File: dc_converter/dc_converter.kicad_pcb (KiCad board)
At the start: 2 copper layers, 58 x 42.5 mm, 39 parts, among them IC1 A3946KLPTR-T, IC2 NCV20072DMR2G, J1 xt30Con, J2 xt30Con, J3 Conn_01x09_Pin, Q1 CSD18531Q5A, Q2 CSD18531Q5A, Q3 CSD18531Q5A, U1 LM74700, U3 INA280A2xDCK, U4 INA280A2xDCK

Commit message: Added 2 simulink concepts, with high and low sides mosfets
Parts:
- R1, R2: footprint Resistor_SMD:R_0402_1005Metric -> Resistor_SMD:R_1206_3216Metric_Pad1.30x1.75mm_HandSolder
- moved R2 15.3 mm to (118.5, 86.5), turned to -90 degrees
- moved R1 10.6 mm to (122.5, 86.5), turned to -90 degrees
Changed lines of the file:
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@@
 		)
 	)
-	(footprint "Resistor_SMD:R_0402_1005Metric"
+	(footprint "Resistor_SMD:R_1206_3216Metric_Pad1.30x1.75mm_HandSolder"
 		(layer "F.Cu")
-		(at 127.5 77.15)
-		(descr "Resistor SMD 0402 (1005 Metric), square (rectangular) end terminal, IPC-7351 nominal, (Body size source: IPC-SM-782 page 72, https://www.pcb-3d.com/wordpress/wp-content/uploads/ipc-sm-782a_amendment_1_and_2.pdf)")
-		(tags "resistor")
+		(at 122.5 86.45 -90)
+		(descr "Resistor SMD 1206 (3216 Metric), square (rectangular) end terminal, IPC-7351 nominal with elongated pad for handsoldering. (Body size source: IPC-SM-782 page 72, https://www.pcb-3d.com/wordpress/wp-content/uploads/ipc-sm-782a_amendment_1_and_2.pdf)")
+		(tags "resistor handsolder")
 		(property "Reference" "R1"
-			(at 2 0 0)
+			(at 0 -1.83 90)
 			(layer "F.SilkS")
 			(effects
@@
 		)
 		(property "Value" "33Ω"
-			(at 0 1.17 0)
+			(at 0 1.83 90)
 			(layer "F.Fab")
 			(effects
@@
 		)
 		(property "Datasheet" ""
-			(at 0 0 0)
+			(at 0 0 90)
 			(layer "F.Fab")
 			(hide yes)
@@
 		)
 		(property "Description" "Resistor"
-			(at 0 0 0)
+			(at 0 0 90)
 			(layer "F.Fab")
 			(hide yes)
@@
 		)
 		(property "KiLib_Generator" "SMD_2terminal_chip_molded"
-			(at 0 0 0)
+			(at 0 0 90)
 			(layer "F.SilkS")
 			(hide yes)
@@
 		(duplicate_pad_numbers_are_jumpers no)
 		(fp_line
-			(start -0.153641 -0.38)
-			(end 0.153641 -0.38)
-			(stroke
-				(width 0.12)
-				(type solid)
-			)
-			(layer "F.SilkS")
-		)
-		(fp_line
-			(start -0.153641 0.38)
-			(end 0.153641 0.38)
+			(start -0.727064 0.91)
+			(end 0.727064 0.91)
+			(stroke
+				(width 0.12)
+				(type solid)
+			)
+			(layer "F.SilkS")
+		)
+		(fp_line
+			(start -0.727064 -0.91)
+			(end 0.727064 -0.91)
 			(stroke
 				(width 0.12)
@@
 		)
 		(fp_rect
-			(start -0.93 -0.47)
-			(end 0.93 0.47)
+			(start -2.45 -1.13)
+			(end 2.45 1.13)
 			(stroke
 				(width 0.05)
@@
 		)
 		(fp_rect
-			(start -0.525 -0.27)
-			(end 0.525 0.27)
+			(start -1.6 -0.8)
+			(end 1.6 0.8)
 			(stroke
 				(width 0.1)
@@
 		)
 		(fp_text user "${REFERENCE}"
-			(at 0 0 0)
-			(layer "F.Fab")
-			(effects
-				(font
-					(size 0.26 0.26)
-					(thickness 0.04)
+			(at 0 0 90)
+			(layer "F.Fab")
+			(effects
+				(font
+					(size 0.8 0.8)
+					(thickness 0.12)
 				)
 			)
 		)
 		(pad "1" smd roundrect
-			(at -0.51 0)
-			(size 0.54 0.64)
-			(layers "F.Cu" "F.Mask" "F.Paste")
-			(roundrect_rratio 0.25)
+			(at -1.55 0 270)
+			(size 1.3 1.75)
+			(layers "F.Cu" "F.Mask" "F.Paste")
+			(roundrect_rratio 0.192308)
 			(net "Net-(IC1-GL)")
 			(pintype "passive")
 		)
 		(pad "2" smd roundrect
-			(at 0.51 0)
-			(size 0.54 0.64)
-			(layers "F.Cu" "F.Mask" "F.Paste")
-			(roundrect_rratio 0.25)
+			(at 1.55 0 270)
+			(size 1.3 1.75)
+			(layers "F.Cu" "F.Mask" "F.Paste")
+			(roundrect_rratio 0.192308)
 			(net "Net-(Q2-G)")
 			(pintype "passive")
 		)
 		(embedded_fonts no)
-		(model "${KICAD10_3DMODEL_DIR}/Resistor_SMD.3dshapes/R_0402_1005Metric.step"
+		(model "${KICAD10_3DMODEL_DIR}/Resistor_SMD.3dshapes/R_1206_3216Metric.step"
 			(offset
 				(xyz 0 0 0)
@@
 		)
 	)
-	(footprint "Resistor_SMD:R_0402_1005Metric"
+	(footprint "Resistor_SMD:R_1206_3216Metric_Pad1.30x1.75mm_HandSolder"
 		(layer "F.Cu")
-		(at 127.5 74.15)
-		(descr "Resistor SMD 0402 (1005 Metric), square (rectangular) end terminal, IPC-7351 nominal, (Body size source: IPC-SM-782 page 72, https://www.pcb-3d.com/wordpress/wp-content/uploads/ipc-sm-782a_amendment_1_and_2.pdf)")
-		(tags "resistor")
+		(at 118.5 86.5 -90)
+		(descr "Resistor SMD 1206 (3216 Metric), square (rectangular) end terminal, IPC-7351 nominal with elongated pad for handsoldering. (Body size source: IPC-SM-782 page 72, https://www.pcb-3d.com/wordpress/wp-content/uploads/ipc-sm-782a_amendment_1_and_2.pdf)")
+		(tags "resistor handsolder")
 		(property "Reference" "R2"
-			(at 2 0 0)
+			(at 0 -1.83 90)
 			(layer "F.SilkS")
 			(effects
@@
 		)
 		(property "Value" "33Ω"
-			(at 0 1.17 0)
+			(at 0 1.83 90)
 			(layer "F.Fab")
 			(effects
@@
 		)
 		(property "Datasheet" ""
-			(at 0 0 0)
+			(at 0 0 90)
 			(layer "F.Fab")
 			(hide yes)
@@
 		)
 		(property "Description" "Resistor"
-			(at 0 0 0)
+			(at 0 0 90)
 			(layer "F.Fab")
 			(hide yes)
@@
 		)
 		(property "KiLib_Generator" "SMD_2terminal_chip_molded"
-			(at 0 0 0)
+			(at 0 0 90)
 			(layer "F.SilkS")
 			(hide yes)
@@
 		(duplicate_pad_numbers_are_jumpers no)
 		(fp_line
-			(start -0.153641 -0.38)
-			(end 0.153641 -0.38)
-			(stroke
-				(width 0.12)
-				(type solid)
-			)
-			(layer "F.SilkS")
-		)
-		(fp_line
-			(start -0.153641 0.38)
-			(end 0.153641 0.38)
+			(start -0.727064 0.91)
+			(end 0.727064 0.91)
+			(stroke
+				(width 0.12)
+				(type solid)
+			)
+			(layer "F.SilkS")
+		)
+		(fp_line
+			(start -0.727064 -0.91)
+			(end 0.727064 -0.91)
 			(stroke
 				(width 0.12)
@@
 		)
 		(fp_rect
-			(start -0.93 -0.47)
-			(end 0.93 0.47)
+			(start -2.45 -1.13)
+			(end 2.45 1.13)
 			(stroke
 				(width 0.05)
@@
 		)
 		(fp_rect
-			(start -0.525 -0.27)
-			(end 0.525 0.27)
+			(start -1.6 -0.8)
+			(end 1.6 0.8)
 			(stroke
 				(width 0.1)
@@
 		)
 		(fp_text user "${REFERENCE}"
-			(at 0 0 0)
-			(layer "F.Fab")
-			(effects
-				(font
-					(size 0.26 0.26)
-					(thickness 0.04)
+			(at 0 0 90)
+			(layer "F.Fab")
+			(effects
+				(font
+					(size 0.8 0.8)
+					(thickness 0.12)
 				)
 			)
 		)
 		(pad "1" smd roundrect
-			(at -0.51 0)
-			(size 0.54 0.64)
-			(layers "F.Cu" "F.Mask" "F.Paste")
-			(roundrect_rratio 0.25)
+			(at -1.55 0 270)
+			(size 1.3 1.75)
+			(layers "F.Cu" "F.Mask" "F.Paste")
+			(roundrect_rratio 0.192308)
 			(net "Net-(IC1-GH)")
 			(pintype "passive")
 		)
 		(pad "2" smd roundrect
-			(at 0.51 0)
-			(size 0.54 0.64)
-			(layers "F.Cu" "F.Mask" "F.Paste")
-			(roundrect_rratio 0.25)
+			(at 1.55 0 270)
+			(size 1.3 1.75)
+			(layers "F.Cu" "F.Mask" "F.Paste")
+			(roundrect_rratio 0.192308)
 			(net "Net-(Q1-G)")
 			(pintype "passive")
 		)
 		(embedded_fonts no)
-		(model "${KICAD10_3DMODEL_DIR}/Resistor_SMD.3dshapes/R_0402_1005Metric.step"
+		(model "${KICAD10_3DMODEL_DIR}/Resistor_SMD.3dshapes/R_1206_3216Metric.step"
 			(offset
 				(xyz 0 0 0)

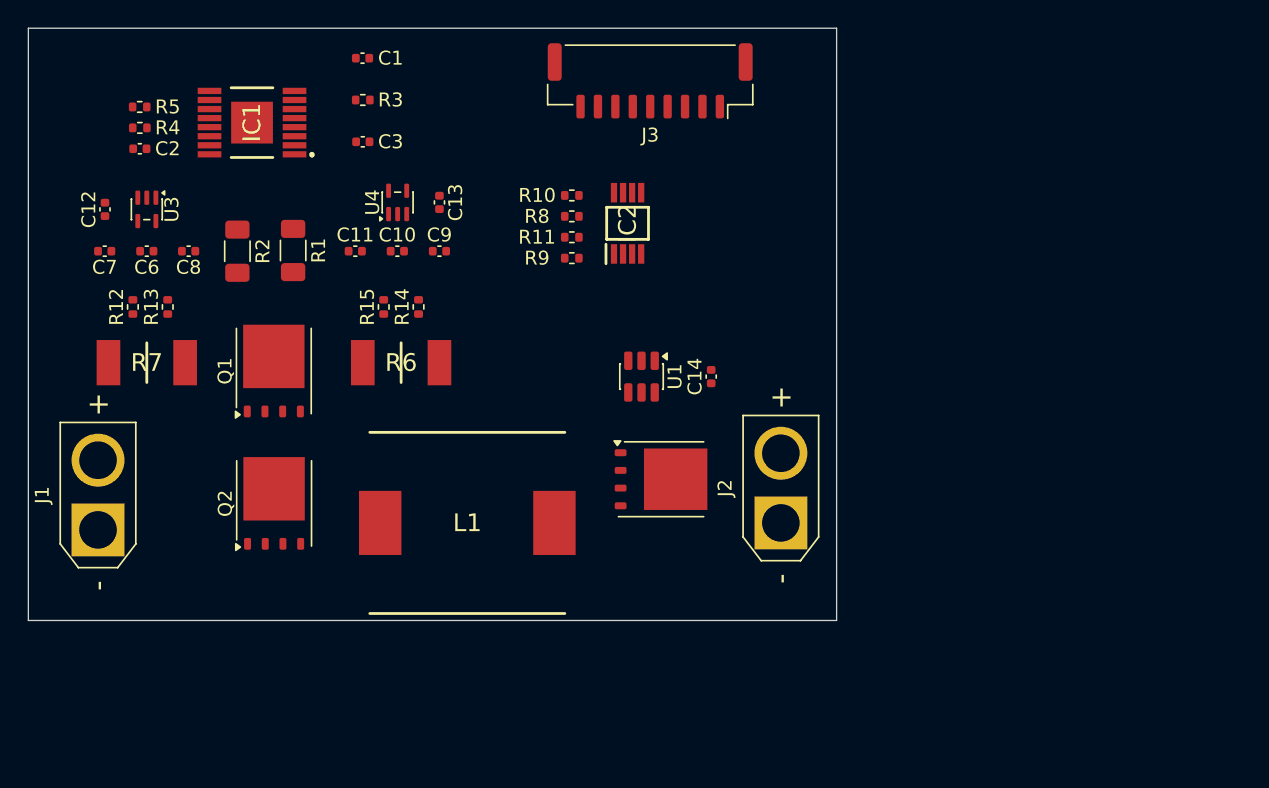
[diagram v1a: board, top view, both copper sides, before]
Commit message: Full topology change to the circuit, diode for Q2, new L, new driver, topology changes in simulink
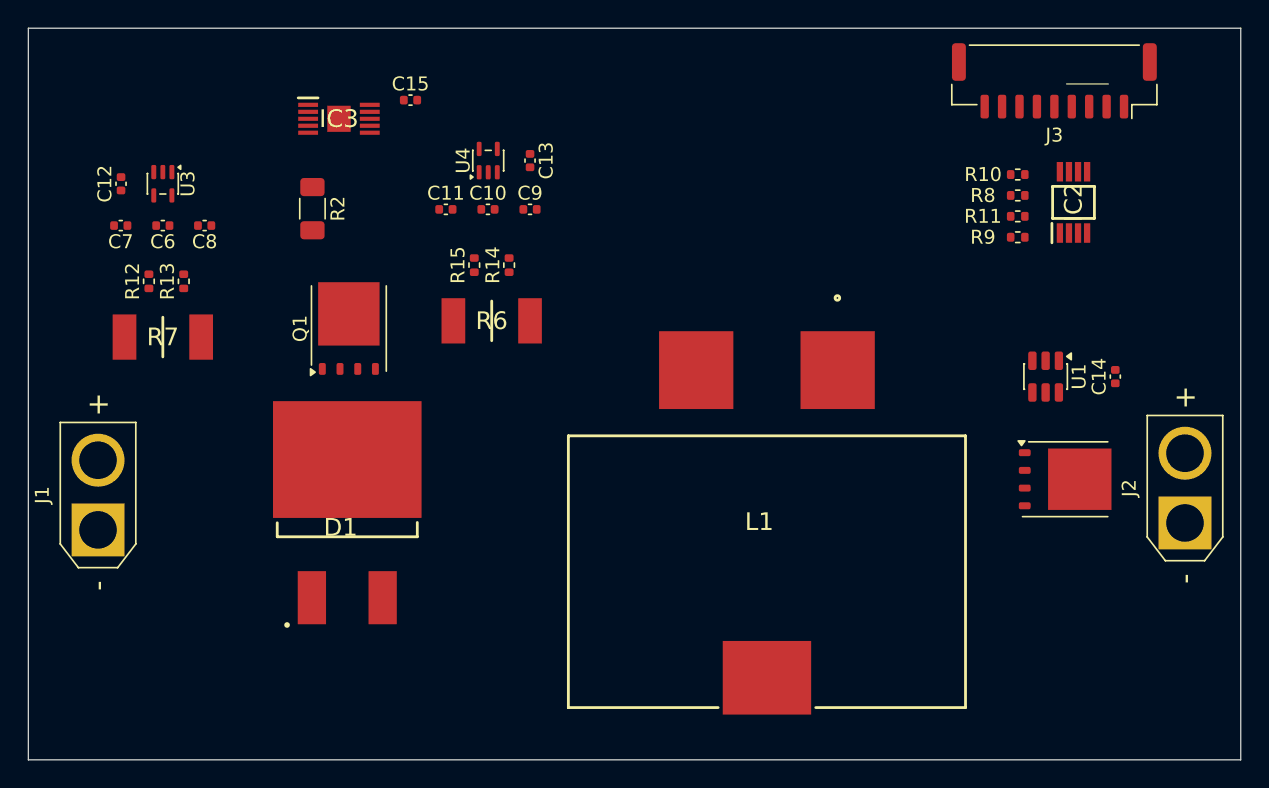
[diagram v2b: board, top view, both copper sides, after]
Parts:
- removed C1, C3: 470nF, Capacitor_SMD:C_0402_1005Metric
- removed C2: 100nF, Capacitor_SMD:C_0402_1005Metric
- removed IC1: A3946KLPTR-T, A3946KLPTR-T:A2550KLPTRT
- removed Q2: CSD18531Q5A, Package_TO_SOT_SMD:TDSON-8-1
- removed R1: 33Ω, Resistor_SMD:R_1206_3216Metric_Pad1.30x1.75mm_HandSolder
- removed R3: 470kΩ, Resistor_SMD:R_0402_1005Metric
- removed R4: 10kΩ, Resistor_SMD:R_0402_1005Metric
- removed R5: 15.8kΩ, Resistor_SMD:R_0402_1005Metric
- added C15: 100nF, Capacitor_SMD:C_0402_1005Metric, F.Cu at (130.9, 75.7)
- added D1: VBT3045C-E3_8W, VBT3045C-E3_8W:TO-263AB_1, F.Cu at (121.4, 98.4)
- added IC3: LTC7004HMSE#TRPBF, LTC7004HMSE:SOP50P490X110-11N, F.Cu at (125.8, 77.0)
- L1: value 744309025 -> 7443641000; footprint 744309025:INDPM140130X900N -> 7443641000:WE-HCF_SMD_HIGH-CURRENT_INDUCTOR
- R2: value 33Ω -> 4.7Ω
- moved IC2 32.0 mm to (178.5, 83.0)
- moved R10 32.0 mm to (174.5, 81.0)
- moved R11 32.0 mm to (174.5, 84.0)
- moved R8 32.0 mm to (174.5, 82.5)
- moved R9 32.0 mm to (174.5, 85.5)
- moved C14 29.0 mm to (181.5, 95.5)
- moved J2 29.0 mm to (186.5, 106.0)
- moved J3 29.0 mm to (177.1, 74.3)
- moved Q3 29.0 mm to (177.9, 102.9)
- moved U1 29.0 mm to (176.5, 95.5)
- moved L1 21.8 mm to (156.5, 109.5)
- moved C11 7.16 mm to (133.5, 83.5)
- moved C10 7.16 mm to (136.5, 83.5)
- moved C13 7.16 mm to (139.5, 80.0)
- moved C9 7.16 mm to (139.5, 83.5)
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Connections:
- J3 pad 2: /T1_in -> unconnected-(J3-Pin_2-Pad2)
- L1 pad 1: Net-(L1-Pad1) -> Net-(U1-ANODE)
- L1 pad 2: Net-(U1-ANODE) -> Net-(L1-Pad2)
- R14 pad 1: Net-(L1-Pad1) -> Net-(L1-Pad2)
- R6 pad 2: Net-(L1-Pad1) -> Net-(L1-Pad2)
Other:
- board size 58 x 42.5 mm -> 87 x 52.5 mm
